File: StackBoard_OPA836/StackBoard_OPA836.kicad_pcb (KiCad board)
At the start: 2 copper layers, 40 x 40 mm, 7 parts, among them IC101 OPA836IDBVT, J101 Conn_01x03_Pin, U101 DoualOutOpAmpGeneric

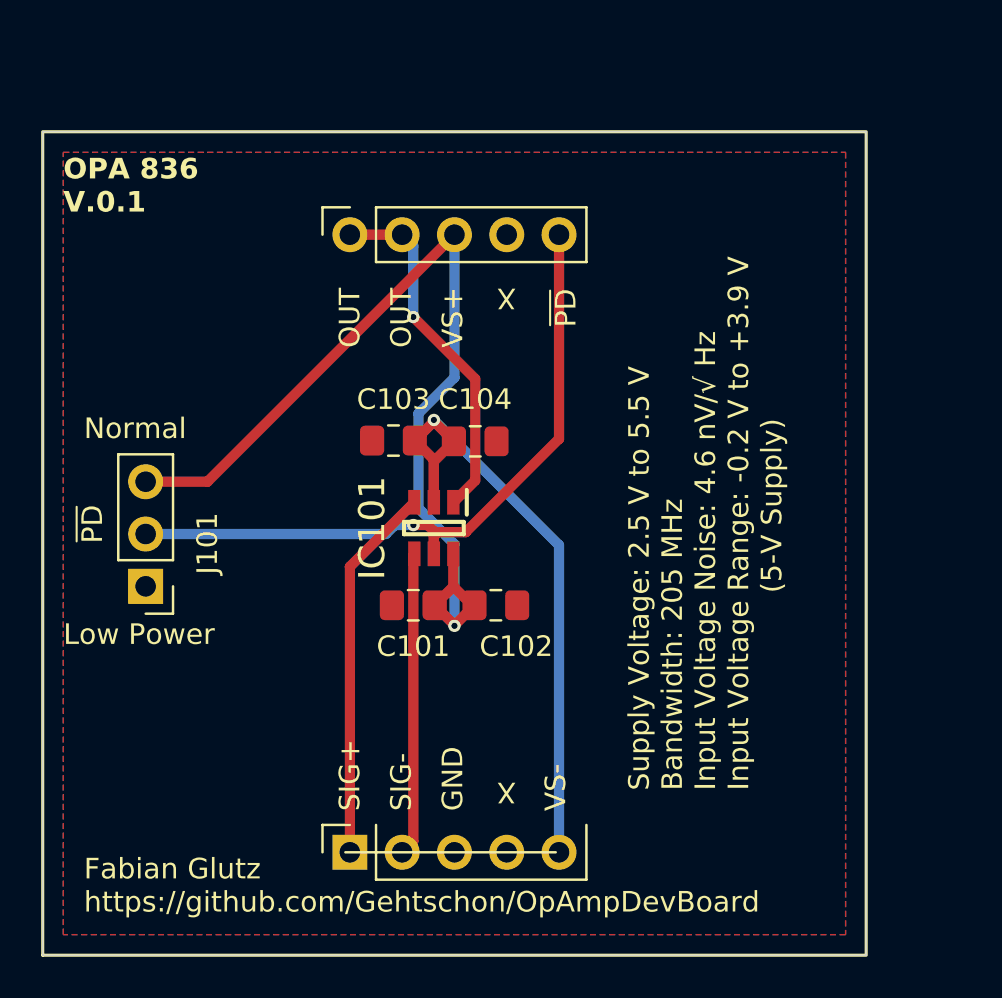
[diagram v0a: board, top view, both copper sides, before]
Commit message: stiching on OPA836 board done
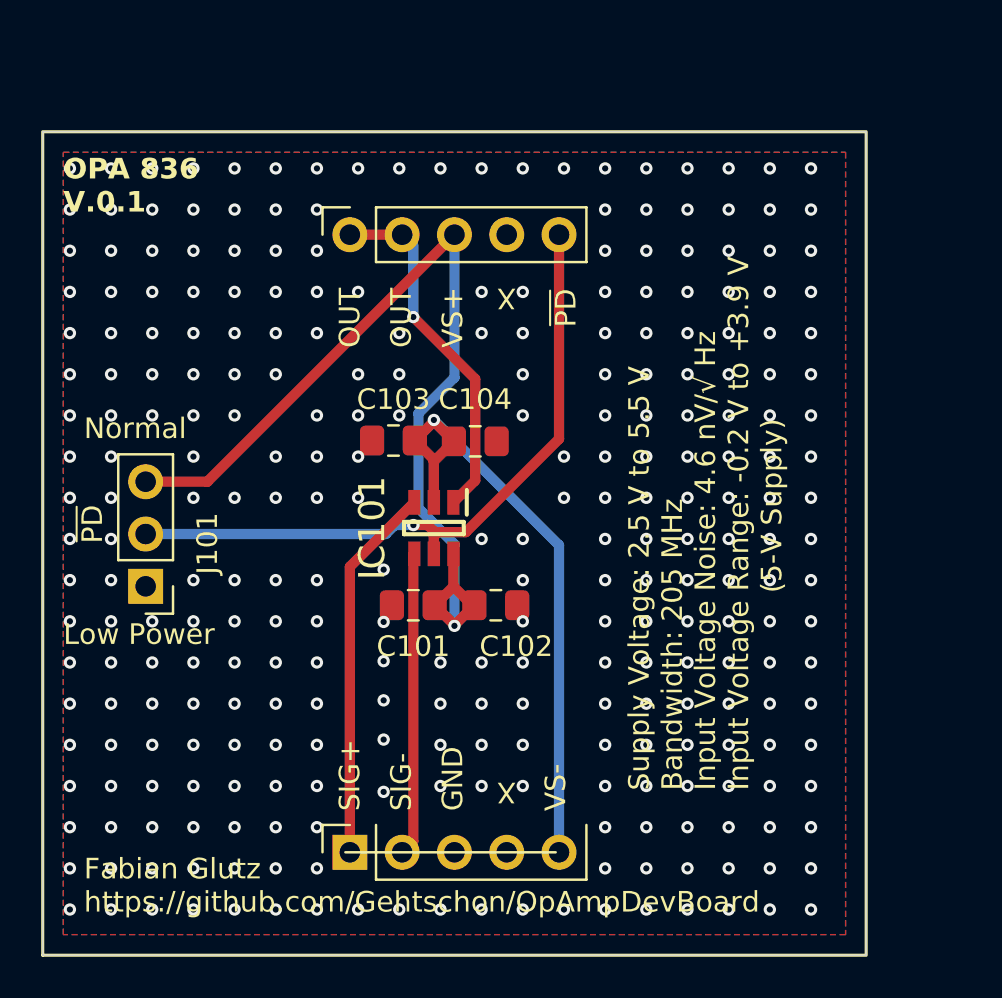
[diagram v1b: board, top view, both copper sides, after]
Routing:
- net GND: vias 0 -> 286
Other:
- board text added: "JLCJLCJLCJLC"
